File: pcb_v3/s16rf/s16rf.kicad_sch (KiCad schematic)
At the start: 105 parts, among them J1 r16_D, J2 r16_C, J3 r16_A, J4 r16_B, J5 r16_C, U1 74LS193, U10 74LS193, U11 74LS193, U12 74LS244, U13 74LS193, U14 74LS244, U15 74LS193, U16 74LS244, U17 74LS244, U18 74LS193, U19 74LS193, U2 74LS193, U20 74LS244, U21 74LS193, U22 74LS244, U23 74LS193, U24 74LS244, U25 74LS244, U26 74LS193, U27 74LS193, U28 74LS244, U29 74LS193, U3 74LS193, U30 74LS244, U31 74LS193, U32 74LS244, U33 74LS244, U34 74LS193, U35 74LS193, U36 74LS244, U37 74LS193, U38 74LS244, U39 74LS193, U4 74LS193, U40 74LS244, U41 74LS574, U42 74LS574, U43 74HC238, U44 74LS574, U45 74LS574, U46 74LS138, U47 74LS574, U49 74LS574, U5 74LS244, U50 74LS574, U6 74LS244, U7 74LS244, U8 74LS244, U9 74LS244

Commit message: avançando o layout da placa com os registradores
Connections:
- net addr_{0}: now also U16.16 (O1a), U24.16 (O1a), U8.16 (O1a); no longer U16.18 (O0a), U24.18 (O0a), U8.18 (O0a)
- net addr_{1}: now also U16.18 (O0a), U24.18 (O0a), U8.18 (O0a); no longer U16.16 (O1a), U24.16 (O1a), U8.16 (O1a)
- net addr_{8}: now also U14.16 (O1a), U22.16 (O1a), U7.16 (O1a); no longer U14.18 (O0a), U22.18 (O0a), U7.18 (O0a)
- net addr_{9}: now also U14.18 (O0a), U22.18 (O0a), U7.18 (O0a); no longer U14.16 (O1a), U22.16 (O1a), U7.16 (O1a)
- net data_{0}: now also U12.16 (O1a), U17.16 (O1a), U20.16 (O1a), U5.16 (O1a), U6.16 (O1a), U9.16 (O1a); no longer U12.18 (O0a), U17.18 (O0a), U20.18 (O0a), U5.18 (O0a), U6.18 (O0a), U9.18 (O0a)
- net data_{1}: now also U12.18 (O0a), U17.18 (O0a), U20.18 (O0a), U5.18 (O0a), U6.18 (O0a), U9.18 (O0a); no longer U12.16 (O1a), U17.16 (O1a), U20.16 (O1a), U5.16 (O1a), U6.16 (O1a), U9.16 (O1a)
- net data_{4}: now also U17.5 (O2b), U5.5 (O2b), U9.5 (O2b); no longer U17.9 (O0b), U5.9 (O0b), U9.9 (O0b)
- net data_{5}: now also U17.3 (O3b), U5.3 (O3b), U9.3 (O3b); no longer U17.7 (O1b), U5.7 (O1b), U9.7 (O1b)
- net data_{6}: now also U17.7 (O1b), U5.7 (O1b), U9.7 (O1b); no longer U17.5 (O2b), U5.5 (O2b), U9.5 (O2b)
- net data_{7}: now also U17.9 (O0b), U5.9 (O0b), U9.9 (O0b); no longer U17.3 (O3b), U5.3 (O3b), U9.3 (O3b)
- net mar_count_{0}: now also U6.4 (I1a), U8.4 (I1a); no longer U6.2 (I0a), U8.2 (I0a)
- net mar_count_{12}: now also U5.15 (I2b); no longer U5.11 (I0b)
- net mar_count_{13}: now also U5.17 (I3b); no longer U5.13 (I1b)
- net mar_count_{14}: now also U5.13 (I1b); no longer U5.15 (I2b)
- net mar_count_{15}: now also U5.11 (I0b); no longer U5.17 (I3b)
- net mar_count_{1}: now also U6.2 (I0a), U8.2 (I0a); no longer U6.4 (I1a), U8.4 (I1a)
- net mar_count_{8}: now also U5.4 (I1a), U7.4 (I1a); no longer U5.2 (I0a), U7.2 (I0a)
- net mar_count_{9}: now also U5.2 (I0a), U7.2 (I0a); no longer U5.4 (I1a), U7.4 (I1a)
- net sp_count_{0}: now also U12.4 (I1a), U16.4 (I1a); no longer U12.2 (I0a), U16.2 (I0a)
- net sp_count_{12}: now also U9.15 (I2b); no longer U9.11 (I0b)
- net sp_count_{13}: now also U9.17 (I3b); no longer U9.13 (I1b)
- net sp_count_{14}: now also U9.13 (I1b); no longer U9.15 (I2b)
- net sp_count_{15}: now also U9.11 (I0b); no longer U9.17 (I3b)
- net sp_count_{1}: now also U12.2 (I0a), U16.2 (I0a); no longer U12.4 (I1a), U16.4 (I1a)
- net sp_count_{8}: now also U14.4 (I1a), U9.4 (I1a); no longer U14.2 (I0a), U9.2 (I0a)
- net sp_count_{9}: now also U14.2 (I0a), U9.2 (I0a); no longer U14.4 (I1a), U9.4 (I1a)
- net zero_count_{0}: now also U20.4 (I1a), U24.4 (I1a); no longer U20.2 (I0a), U24.2 (I0a)
- net zero_count_{12}: now also U17.15 (I2b); no longer U17.11 (I0b)
- net zero_count_{13}: now also U17.17 (I3b); no longer U17.13 (I1b)
- net zero_count_{14}: now also U17.13 (I1b); no longer U17.15 (I2b)
- net zero_count_{15}: now also U17.11 (I0b); no longer U17.17 (I3b)
- net zero_count_{1}: now also U20.2 (I0a), U24.2 (I0a); no longer U20.4 (I1a), U24.4 (I1a)
- net zero_count_{8}: now also U17.4 (I1a), U22.4 (I1a); no longer U17.2 (I0a), U22.2 (I0a)
- net zero_count_{9}: now also U17.2 (I0a), U22.2 (I0a); no longer U17.4 (I1a), U22.4 (I1a)

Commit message: finalização da primeira fase de layout do pcb
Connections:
- net addr_{0}: now also U32.16 (O1a), U40.16 (O1a); no longer U32.18 (O0a), U40.18 (O0a)
- net addr_{1}: now also U32.18 (O0a), U40.18 (O0a); no longer U32.16 (O1a), U40.16 (O1a)
- net addr_{8}: now also U30.16 (O1a), U38.16 (O1a); no longer U30.18 (O0a), U38.18 (O0a)
- net addr_{9}: now also U30.18 (O0a), U38.18 (O0a); no longer U30.16 (O1a), U38.16 (O1a)
- net data_{0}: now also U25.16 (O1a), U28.16 (O1a), U33.16 (O1a), U36.16 (O1a); no longer U25.18 (O0a), U28.18 (O0a), U33.18 (O0a), U36.18 (O0a)
- net data_{1}: now also U25.18 (O0a), U28.18 (O0a), U33.18 (O0a), U36.18 (O0a); no longer U25.16 (O1a), U28.16 (O1a), U33.16 (O1a), U36.16 (O1a)
- net data_{4}: now also U25.5 (O2b), U33.5 (O2b); no longer U25.9 (O0b), U33.9 (O0b)
- net data_{5}: now also U25.3 (O3b), U33.3 (O3b); no longer U25.7 (O1b), U33.7 (O1b)
- net data_{6}: now also U25.7 (O1b), U33.7 (O1b); no longer U25.5 (O2b), U33.5 (O2b)
- net data_{7}: now also U25.9 (O0b), U33.9 (O0b); no longer U25.3 (O3b), U33.3 (O3b)
- net one_count_{0}: now also U28.4 (I1a), U32.4 (I1a); no longer U28.2 (I0a), U32.2 (I0a)
- net one_count_{12}: now also U25.15 (I2b); no longer U25.11 (I0b)
- net one_count_{13}: now also U25.17 (I3b); no longer U25.13 (I1b)
- net one_count_{14}: now also U25.13 (I1b); no longer U25.15 (I2b)
- net one_count_{15}: now also U25.11 (I0b); no longer U25.17 (I3b)
- net one_count_{1}: now also U28.2 (I0a), U32.2 (I0a); no longer U28.4 (I1a), U32.4 (I1a)
- net one_count_{8}: now also U25.4 (I1a), U30.4 (I1a); no longer U25.2 (I0a), U30.2 (I0a)
- net one_count_{9}: now also U25.2 (I0a), U30.2 (I0a); no longer U25.4 (I1a), U30.4 (I1a)
- net two_count_{0}: now also U36.4 (I1a), U40.4 (I1a); no longer U36.2 (I0a), U40.2 (I0a)
- net two_count_{12}: now also U33.15 (I2b); no longer U33.11 (I0b)
- net two_count_{13}: now also U33.17 (I3b); no longer U33.13 (I1b)
- net two_count_{14}: now also U33.13 (I1b); no longer U33.15 (I2b)
- net two_count_{15}: now also U33.11 (I0b); no longer U33.17 (I3b)
- net two_count_{1}: now also U36.2 (I0a), U40.2 (I0a); no longer U36.4 (I1a), U40.4 (I1a)
- net two_count_{8}: now also U33.4 (I1a), U38.4 (I1a); no longer U33.2 (I0a), U38.2 (I0a)
- net two_count_{9}: now also U33.2 (I0a), U38.2 (I0a); no longer U33.4 (I1a), U38.4 (I1a)

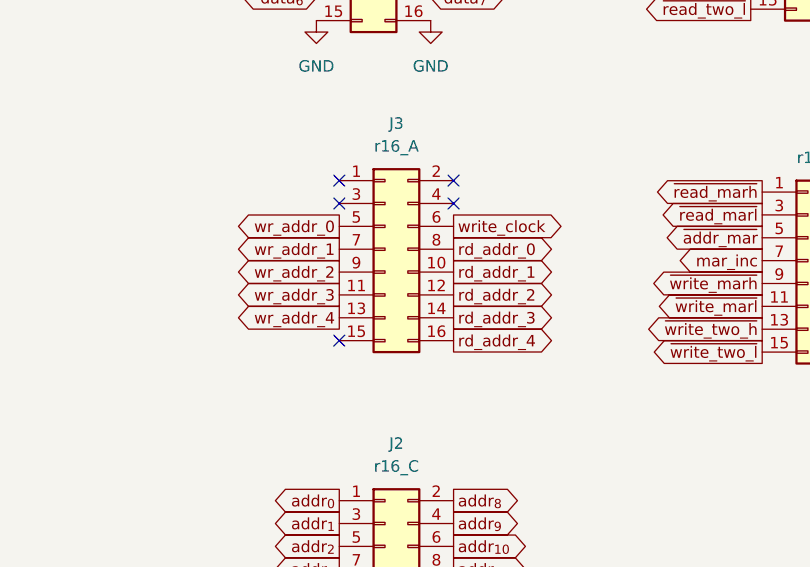
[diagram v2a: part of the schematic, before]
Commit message: avançado na otimização do pcb
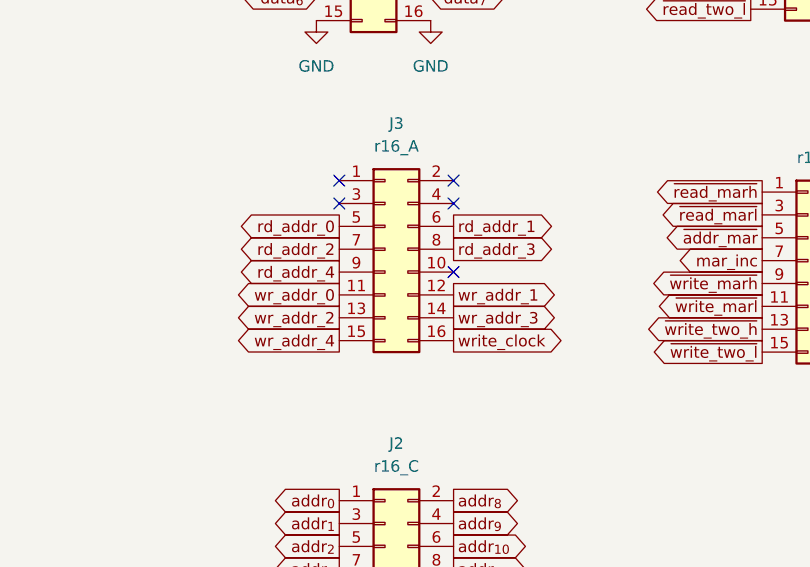
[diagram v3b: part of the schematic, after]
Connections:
- net rd_addr_0: now also J3.5 (Pin_5); no longer J3.8 (Pin_8)
- net rd_addr_1: now also J3.6 (Pin_6); no longer J3.10 (Pin_10)
- net rd_addr_2: now also J3.7 (Pin_7); no longer J3.12 (Pin_12)
- net rd_addr_3: now also J3.8 (Pin_8); no longer J3.14 (Pin_14)
- net rd_addr_4: now also J3.9 (Pin_9); no longer J3.16 (Pin_16)
- net wr_addr_0: now also J3.11 (Pin_11); no longer J3.5 (Pin_5)
- net wr_addr_1: now also J3.12 (Pin_12); no longer J3.7 (Pin_7)
- net wr_addr_2: now also J3.13 (Pin_13); no longer J3.9 (Pin_9)
- net wr_addr_3: now also J3.14 (Pin_14); no longer J3.11 (Pin_11)
- net wr_addr_4: now also J3.15 (Pin_15); no longer J3.13 (Pin_13)
- net write_clock: now also J3.16 (Pin_16); no longer J3.6 (Pin_6)

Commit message: concluida a primeira rodada de layout do pcb; removidas conexões de cascateamento de decremento para os registradores que não tenham esta função
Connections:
- net +5V: now also U1.4 (DOWN), U18.4 (DOWN), U19.4 (DOWN), U2.4 (DOWN), U21.4 (DOWN), U26.4 (DOWN), U27.4 (DOWN), U29.4 (DOWN), U3.4 (DOWN), U34.4 (DOWN), U35.4 (DOWN), U37.4 (DOWN)
- net mar_borrow_2: no longer names the net of U4.13 (~{BO})
- net mar_borrow_2: no longer U3.4 (DOWN)
- net mar_borrow_3: no longer names the net of U3.13 (~{BO})
- net mar_borrow_3: no longer U2.4 (DOWN)
- net mar_borrow_4: no longer names the net of U2.13 (~{BO})
- net mar_borrow_4: no longer U1.4 (DOWN)
- net one_borrow_2: no longer names the net of U31.13 (~{BO})
- net one_borrow_2: no longer U29.4 (DOWN)
- net one_borrow_3: no longer names the net of U29.13 (~{BO})
- net one_borrow_3: no longer U27.4 (DOWN)
- net one_borrow_4: no longer names the net of U27.13 (~{BO})
- net one_borrow_4: no longer U26.4 (DOWN)
- net two_borrow_2: no longer names the net of U39.13 (~{BO})
- net two_borrow_2: no longer U37.4 (DOWN)
- net two_borrow_3: no longer names the net of U37.13 (~{BO})
- net two_borrow_3: no longer U35.4 (DOWN)
- net two_borrow_4: no longer names the net of U35.13 (~{BO})
- net two_borrow_4: no longer U34.4 (DOWN)
- net zero_borrow_2: no longer names the net of U23.13 (~{BO})
- net zero_borrow_2: no longer U21.4 (DOWN)
- net zero_borrow_3: no longer names the net of U21.13 (~{BO})
- net zero_borrow_3: no longer U19.4 (DOWN)
- net zero_borrow_4: no longer names the net of U19.13 (~{BO})
- net zero_borrow_4: no longer U18.4 (DOWN)
- no-connect marks 22 -> 34
